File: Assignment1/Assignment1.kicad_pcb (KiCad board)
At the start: 2 copper layers, 50 x 50 mm, 22 parts, among them J1 Conn_01x02_Pin, J2 Conn_01x02_Pin, U1 TPS51386RJNR, U2 LD39200PU33R

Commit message: Update Assignment 1
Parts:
- removed Cbyp1: 470 nF, Capacitor_SMD:C_0603_1608Metric
- removed Cin1, Cout1: 10 uF, Capacitor_SMD:C_0603_1608Metric
- removed R_LDO_1: 56k, Resistor_SMD:R_0603_1608Metric
- removed R_LDO_2: 10k, Resistor_SMD:R_0603_1608Metric
- removed U2: LD39200PU33R, LD39200PU33R:SON95P300X300X100-7N
- added C2: 22pF, Capacitor_SMD:C_1210_3225Metric, F.Cu at (91.9, 83.8)
- added C3: 22pF, Capacitor_SMD:C_1210_3225Metric, F.Cu at (91.9, 80.3)
- added C8: 22pF, Capacitor_SMD:C_1210_3225Metric, F.Cu at (85.6, 83.9)
- added Cbyp2: 47 uF, Capacitor_SMD:C_1206_3216Metric, F.Cu at (73.3, 75.5)
- added Cin2: 1 uF, Capacitor_SMD:C_0603_1608Metric, F.Cu at (75.7, 85.1)
- added U3: ~, Package_TO_SOT_SMD:TO-263-3_TabPin2, F.Cu at (61.9, 83.3)
- C12: footprint Capacitor_SMD:C_0603_1608Metric -> Capacitor_SMD:C_1210_3225Metric
- C4, C5: footprint Capacitor_SMD:C_0603_1608Metric -> Capacitor_SMD:C_1206_3216Metric
- C7: value 100uF -> 22pF; footprint Capacitor_SMD:C_0603_1608Metric -> Capacitor_SMD:C_1210_3225Metric
- J1, J2: footprint Connector_PinSocket_2.54mm:PinSocket_1x02_P2.54mm_Vertical -> 5EHDVC-02P-KiCad:5EHDVC02P
- R4: value 150k -> 110k
- moved J1 38.3 mm to (89.6, 56.9), turned to 180 degrees
- moved C4 31.1 mm to (88.0, 63.3), turned to 180 degrees
- moved R3 29.2 mm to (93.3, 68.8), turned to 180 degrees
- moved C13 28.8 mm to (95.0, 70.6), turned to 0 degrees
- moved C5 28.3 mm to (88.0, 66.4), turned to 180 degrees
- moved J2 28.0 mm to (64.8, 56.5), turned to 0 degrees
- moved R1 27.1 mm to (95.1, 72.4), turned to 0 degrees
- moved C6 26.4 mm to (88.6, 68.6), turned to 180 degrees
- moved C1 26.1 mm to (95.2, 74.7), turned to 180 degrees
- moved U1 23.5 mm to (89.0, 71.7), turned to -90 degrees
- moved R6 19.5 mm to (81.0, 66.5)
- moved L1 19.3 mm to (88.9, 76.0), turned to -90 degrees
- moved R5 16.3 mm to (81.1, 68.8), turned to 180 degrees
- moved C7 15.4 mm to (85.6, 80.3), turned to 180 degrees
- moved R4 11.9 mm to (81.1, 71.4), turned to 180 degrees
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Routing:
- net /Buck_Vin: track 10.8 -> 0.00 mm
- net /Vout: track 9.98 -> 0.00 mm
- net Net-(U2-SENSE): track 7.18 -> 0.00 mm
- net /Buck_SW: track 6.28 -> 1.19 mm
- net Earth: track 7.67 -> 4.24 mm, vias 12 -> 36
- net /BuckStep_Vout: track 11.8 -> 14.3 mm
- net /Buck_VBST: track 3.27 -> 5.75 mm
- net /Buck_FB: track 8.46 -> 10.6 mm
- net /Buck_PG: track 10.3 -> 11.1 mm
- net Net-(C1-Pad1): track 1.80 -> 2.34 mm
- added copper zone on F.Cu, net /BuckStep_Vout
- added copper zone on F.Cu, net /Buck_SW
- added copper zone on F.Cu, net /Buck_Vin
- added copper zone on F.Cu, net /Vout

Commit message: fix smt
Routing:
- net /BuckStep_Vout: track 14.3 -> 0.00 mm
- net /Buck_PG: track 11.1 -> 0.00 mm, vias 2 -> 0
- net /Buck_FB: track 10.6 -> 0.00 mm
- net /Buck_Vcc: track 6.48 -> 0.00 mm
- net /Buck_VBST: track 5.75 -> 0.00 mm
- net Earth: track 4.24 -> 0.00 mm, vias 36 -> 0
- net Net-(C12-Pad1): track 3.06 -> 0.00 mm
- net Net-(C1-Pad1): track 2.34 -> 0.00 mm
- net /Buck_SW: track 1.19 -> 0.00 mm
- removed copper zone on F.Cu, net /BuckStep_Vout
- removed copper zone on F.Cu, net /Buck_SW
- removed copper zone on F.Cu, net /Buck_Vin
- removed copper zone on F.Cu, net /Vout
- removed copper zone on B.Cu, net Earth
- removed copper zone on F.Cu, net Earth

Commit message: generate BOM
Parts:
- moved Cbyp2 9.62 mm to (68.0, 67.5)
- moved U3 3.58 mm to (59.4, 80.8)
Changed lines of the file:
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@@
 	(footprint "Package_TO_SOT_SMD:TO-263-3_TabPin2"
 		(layer "F.Cu")
-		(at 61.946 83.312 180)
+		(at 59.425 80.775 180)
 		(descr "TO-263/D2PAK/DDPAK SMD package, http://www.infineon.com/cms/en/product/packages/PG-TO263/PG-TO263-3-1/")
 		(tags "D2PAK DDPAK TO-263 D2PAK-3 TO-263-3 SOT-404")
@@
 	(footprint "Capacitor_SMD:C_1206_3216Metric"
 		(layer "F.Cu")
-		(at 73.2518 75.5396)
+		(at 67.975 67.5)
 		(descr "Capacitor SMD 1206 (3216 Metric), square (rectangular) end terminal, IPC_7351 nominal, (Body size source: IPC-SM-782 page 76, https://www.pcb-3d.com/wordpress/wp-content/uploads/ipc-sm-782a_amendment_1_and_2.pdf), generated with kicad-footprint-generator")
 		(tags "capacitor")

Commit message: fix typo and update pcb
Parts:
- C2, C3, C7, C8: value 22pF -> 22uF
- moved C2 7.77 mm to (93.1, 91.5)
- moved C8 7.70 mm to (86.8, 91.5)
- moved C3 5.37 mm to (93.1, 85.5)
- moved C7 5.16 mm to (85.7, 85.5)
- moved R4 4.56 mm to (78.3, 75.0)
- moved C12 4.47 mm to (73.0, 71.0)
- moved C1 4.01 mm to (96.5, 78.5)
- moved L1 3.97 mm to (89.7, 79.9)
- moved U1 3.66 mm to (89.9, 75.2)
- moved C6 3.21 mm to (90.8, 71.0)
- moved R5 2.84 mm to (78.3, 69.5)
- moved R3 2.78 mm to (96.0, 68.0)
- moved R1 2.63 mm to (95.3, 75.0)
- moved C5 2.03 mm to (90.0, 67.0)
- moved R6 1.07 mm to (82.0, 67.0)
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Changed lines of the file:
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@@
 	(footprint "Resistor_SMD:R_0603_1608Metric"
 		(layer "F.Cu")
-		(at 93.345 68.834 180)
+		(at 96 68 180)
 		(descr "Resistor SMD 0603 (1608 Metric), square (rectangular) end terminal, IPC_7351 nominal, (Body size source: IPC-SM-782 page 72, https://www.pcb-3d.com/wordpress/wp-content/uploads/ipc-sm-782a_amendment_1_and_2.pdf), generated with kicad-footprint-generator")
 		(tags "resistor")
 		(property "Reference" "R3"
-			(at -2.667 0 0)
+			(at -0.675 1.5 0)
 			(layer "F.SilkS")
 			(effects
@@
 	(footprint "Capacitor_SMD:C_0603_1608Metric"
 		(layer "F.Cu")
-		(at 95.237 74.676 180)
+		(at 96.45 78.5 180)
 		(descr "Capacitor SMD 0603 (1608 Metric), square (rectangular) end terminal, IPC_7351 nominal, (Body size source: IPC-SM-782 page 76, https://www.pcb-3d.com/wordpress/wp-content/uploads/ipc-sm-782a_amendment_1_and_2.pdf), generated with kicad-footprint-generator")
 		(tags "capacitor")
@@
 	(footprint "Capacitor_SMD:C_1210_3225Metric"
 		(layer "F.Cu")
-		(at 85.607 83.893 180)
+		(at 86.782 91.5 180)
 		(descr "Capacitor SMD 1210 (3225 Metric), square (rectangular) end terminal, IPC_7351 nominal, (Body size source: IPC-SM-782 page 76, https://www.pcb-3d.com/wordpress/wp-content/uploads/ipc-sm-782a_amendment_1_and_2.pdf), generated with kicad-footprint-generator")
 		(tags "capacitor")
@@
 			)
 		)
-		(property "Value" "22pF"
+		(property "Value" "22uF"
 			(at 0 2.3 0)
 			(layer "F.Fab")
@@
 	(footprint "Resistor_SMD:R_0603_1608Metric"
 		(layer "F.Cu")
-		(at 81.09 68.834 180)
+		(at 78.325 69.5 180)
 		(descr "Resistor SMD 0603 (1608 Metric), square (rectangular) end terminal, IPC_7351 nominal, (Body size source: IPC-SM-782 page 72, https://www.pcb-3d.com/wordpress/wp-content/uploads/ipc-sm-782a_amendment_1_and_2.pdf), generated with kicad-footprint-generator")
 		(tags "resistor")
 		(property "Reference" "R5"
-			(at -2.603 0 0)
+			(at -3.778 -2.5 0)
 			(layer "F.SilkS")
 			(effects
@@
 		)
 		(property "Value" "0"
-			(at 0 1.43 0)
+			(at -1.175 -1.07 0)
 			(layer "F.Fab")
 			(effects
@@
 		)
 		(fp_text user "${REFERENCE}"
-			(at 0 0 0)
+			(at -1.175 -2.5 0)
 			(layer "F.Fab")
 			(effects
@@
 	(footprint "Capacitor_SMD:C_1210_3225Metric"
 		(layer "F.Cu")
-		(at 85.607 80.337 180)
+		(at 85.65 85.5 180)
 		(descr "Capacitor SMD 1210 (3225 Metric), square (rectangular) end terminal, IPC_7351 nominal, (Body size source: IPC-SM-782 page 76, https://www.pcb-3d.com/wordpress/wp-content/uploads/ipc-sm-782a_amendment_1_and_2.pdf), generated with kicad-footprint-generator")
 		(tags "capacitor")
@@
 			)
 		)
-		(property "Value" "22pF"
+		(property "Value" "22uF"
 			(at 0 2.3 0)
 			(layer "F.Fab")
@@
 	(footprint "Capacitor_SMD:C_1210_3225Metric"
 		(layer "F.Cu")
-		(at 91.948 83.82)
+		(at 93.123 91.5)
 		(descr "Capacitor SMD 1210 (3225 Metric), square (rectangular) end terminal, IPC_7351 nominal, (Body size source: IPC-SM-782 page 76, https://www.pcb-3d.com/wordpress/wp-content/uploads/ipc-sm-782a_amendment_1_and_2.pdf), generated with kicad-footprint-generator")
 		(tags "capacitor")
@@
 			)
 		)
-		(property "Value" "22pF"
+		(property "Value" "22uF"
 			(at 0 2.3 0)
 			(layer "F.Fab")
@@
 	(footprint "Capacitor_SMD:C_1210_3225Metric"
 		(layer "F.Cu")
-		(at 77.343 69.977 -90)
+		(at 73 71.025 -90)
 		(descr "Capacitor SMD 1210 (3225 Metric), square (rectangular) end terminal, IPC_7351 nominal, (Body size source: IPC-SM-782 page 76, https://www.pcb-3d.com/wordpress/wp-content/uploads/ipc-sm-782a_amendment_1_and_2.pdf), generated with kicad-footprint-generator")
 		(tags "capacitor")
@@
 	(footprint "Resistor_SMD:R_0603_1608Metric"
 		(layer "F.Cu")
-		(at 95.059 72.39)
+		(at 95.35 75)
 		(descr "Resistor SMD 0603 (1608 Metric), square (rectangular) end terminal, IPC_7351 nominal, (Body size source: IPC-SM-782 page 72, https://www.pcb-3d.com/wordpress/wp-content/uploads/ipc-sm-782a_amendment_1_and_2.pdf), generated with kicad-footprint-generator")
 		(tags "resistor")
@@
 	(footprint "Inductor_SMD:L_1210_3225Metric"
 		(layer "F.Cu")
-		(at 88.86 76.019 -90)
+		(at 89.675 79.9 -90)
 		(descr "Inductor SMD 1210 (3225 Metric), square (rectangular) end terminal, IPC_7351 nominal, (Body size source: http://www.tortai-tech.com/upload/download/2011102023233369053.pdf), generated with kicad-footprint-generator")
 		(tags "inductor")
@@
 	(footprint "Capacitor_SMD:C_1206_3216Metric"
 		(layer "F.Cu")
-		(at 88.049 66.367 180)
+		(at 89.975 67 180)
 		(descr "Capacitor SMD 1206 (3216 Metric), square (rectangular) end terminal, IPC_7351 nominal, (Body size source: IPC-SM-782 page 76, https://www.pcb-3d.com/wordpress/wp-content/uploads/ipc-sm-782a_amendment_1_and_2.pdf), generated with kicad-footprint-generator")
 		(tags "capacitor")
@@
 	(footprint "Capacitor_SMD:C_0603_1608Metric"
 		(layer "F.Cu")
-		(at 88.606 68.6308 180)
+		(at 90.775 71 180)
 		(descr "Capacitor SMD 0603 (1608 Metric), square (rectangular) end terminal, IPC_7351 nominal, (Body size source: IPC-SM-782 page 76, https://www.pcb-3d.com/wordpress/wp-content/uploads/ipc-sm-782a_amendment_1_and_2.pdf), generated with kicad-footprint-generator")
 		(tags "capacitor")
@@
 		)
 		(property "Value" "0.1 uF"
-			(at 3.797 -0.762 90)
+			(at 2.275 0 90)
 			(layer "F.Fab")
 			(effects
@@
 	(footprint "Capacitor_SMD:C_1210_3225Metric"
 		(layer "F.Cu")
-		(at 91.899 80.264)
+		(at 93.074 85.5)
 		(descr "Capacitor SMD 1210 (3225 Metric), square (rectangular) end terminal, IPC_7351 nominal, (Body size source: IPC-SM-782 page 76, https://www.pcb-3d.com/wordpress/wp-content/uploads/ipc-sm-782a_amendment_1_and_2.pdf), generated with kicad-footprint-generator")
 		(tags "capacitor")
@@
 			)
 		)
-		(property "Value" "22pF"
+		(property "Value" "22uF"
 			(at 0 2.3 0)
 			(layer "F.Fab")
@@
 	(footprint "Resistor_SMD:R_0603_1608Metric"
 		(layer "F.Cu")
-		(at 81.026 66.548)
+		(at 82 67)
 		(descr "Resistor SMD 0603 (1608 Metric), square (rectangular) end terminal, IPC_7351 nominal, (Body size source: IPC-SM-782 page 72, https://www.pcb-3d.com/wordpress/wp-content/uploads/ipc-sm-782a_amendment_1_and_2.pdf), generated with kicad-footprint-generator")
 		(tags "resistor")
@@
 	(footprint "TPS51386RJNR:VREG_TPS51386RJNR"
 		(layer "F.Cu")
-		(at 88.99 71.701 -90)
+		(at 89.9 75.25 -90)
 		(property "Reference" "U1"
 			(at -0.008 3.048 90)
@@
 		)
 		(property "Value" "TPS51386RJNR"
-			(at 0.5 5.842 90)
+			(at 0.25 4.4 90)
 			(layer "F.Fab")
 			(effects
@@
 	(footprint "Capacitor_SMD:C_0603_1608Metric"
 		(layer "F.Cu")
-		(at 94.983 70.612)
+		(at 95.45 71.5)
 		(descr "Capacitor SMD 0603 (1608 Metric), square (rectangular) end terminal, IPC_7351 nominal, (Body size source: IPC-SM-782 page 76, https://www.pcb-3d.com/wordpress/wp-content/uploads/ipc-sm-782a_amendment_1_and_2.pdf), generated with kicad-footprint-generator")
 		(tags "capacitor")
@@
 		)
 		(fp_text user "${REFERENCE}"
-			(at 0 0 0)
+			(at -1.175 -2.5 0)
 			(layer "F.Fab")
 			(effects
@@
 	(footprint "Resistor_SMD:R_0603_1608Metric"
 		(layer "F.Cu")
-		(at 81.089 71.374 180)
+		(at 78.325 75 180)
 		(descr "Resistor SMD 0603 (1608 Metric), square (rectangular) end terminal, IPC_7351 nominal, (Body size source: IPC-SM-782 page 72, https://www.pcb-3d.com/wordpress/wp-content/uploads/ipc-sm-782a_amendment_1_and_2.pdf), generated with kicad-footprint-generator")
 		(tags "resistor")
 		(property "Reference" "R4"
-			(at -2.604 0.127 0)
+			(at -3.779 -2.373 0)
 			(layer "F.SilkS")
 			(effects
@@
 		)
 		(fp_text user "${REFERENCE}"
-			(at 0 0 0)
+			(at -1.175 -2.5 0)
 			(layer "F.Fab")
 			(effects

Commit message: reformat
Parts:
- C13, Cin2: value 1 uF -> 1uF
- C4, C5: value 10 uF -> 10uF
- C6: value 0.1 uF -> 0.1uF
- Cbyp2: value 47 uF -> 47uF
- R3: value 100 k -> 100k
- moved C1 0.84 mm to (95.8, 79.0)
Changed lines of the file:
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@@
 			)
 		)
-		(property "Value" "100 k"
+		(property "Value" "100k"
 			(at -3.747 0 0)
 			(layer "F.Fab")
@@
 	(footprint "Capacitor_SMD:C_0603_1608Metric"
 		(layer "F.Cu")
-		(at 96.45 78.5 180)
+		(at 95.775 79 180)
 		(descr "Capacitor SMD 0603 (1608 Metric), square (rectangular) end terminal, IPC_7351 nominal, (Body size source: IPC-SM-782 page 76, https://www.pcb-3d.com/wordpress/wp-content/uploads/ipc-sm-782a_amendment_1_and_2.pdf), generated with kicad-footprint-generator")
 		(tags "capacitor")
@@
 		(tags "resistor")
 		(property "Reference" "R5"
-			(at -3.778 -2.5 0)
+			(at -0.175 1.5 0)
 			(layer "F.SilkS")
 			(effects
@@
 		)
 		(property "Value" "0"
-			(at -1.175 -1.07 0)
+			(at -0.175 -1.5 0)
 			(layer "F.Fab")
 			(effects
@@
 		)
 		(fp_text user "${REFERENCE}"
-			(at -1.175 -2.5 0)
+			(at 0 0 0)
 			(layer "F.Fab")
 			(effects
@@
 			)
 		)
-		(property "Value" "10 uF"
+		(property "Value" "10uF"
 			(at 2.999 0 90)
 			(layer "F.Fab")
@@
 			)
 		)
-		(property "Value" "0.1 uF"
+		(property "Value" "0.1uF"
 			(at 2.275 0 90)
 			(layer "F.Fab")
@@
 			)
 		)
-		(property "Value" "1 uF"
+		(property "Value" "1uF"
 			(at 0 1.43 0)
 			(layer "F.Fab")
@@
 			)
 		)
-		(property "Value" "1 uF"
+		(property "Value" "1uF"
 			(at 0 1.43 90)
 			(layer "F.Fab")
@@
 			)
 		)
-		(property "Value" "10 uF"
+		(property "Value" "10uF"
 			(at 2.999 0 90)
 			(layer "F.Fab")
@@
 		)
 		(fp_text user "${REFERENCE}"
-			(at -1.175 -2.5 0)
+			(at 0 0 0)
 			(layer "F.Fab")
 			(effects
@@
 			)
 		)
-		(property "Value" "47 uF"
+		(property "Value" "47uF"
 			(at 0 1.85 0)
 			(layer "F.Fab")
@@
 		(tags "resistor")
 		(property "Reference" "R4"
-			(at -3.779 -2.373 0)
+			(at -0.175 -1.5 0)
 			(layer "F.SilkS")
 			(effects
@@
 		)
 		(fp_text user "${REFERENCE}"
-			(at -1.175 -2.5 0)
+			(at 0 0 0)
 			(layer "F.Fab")
 			(effects

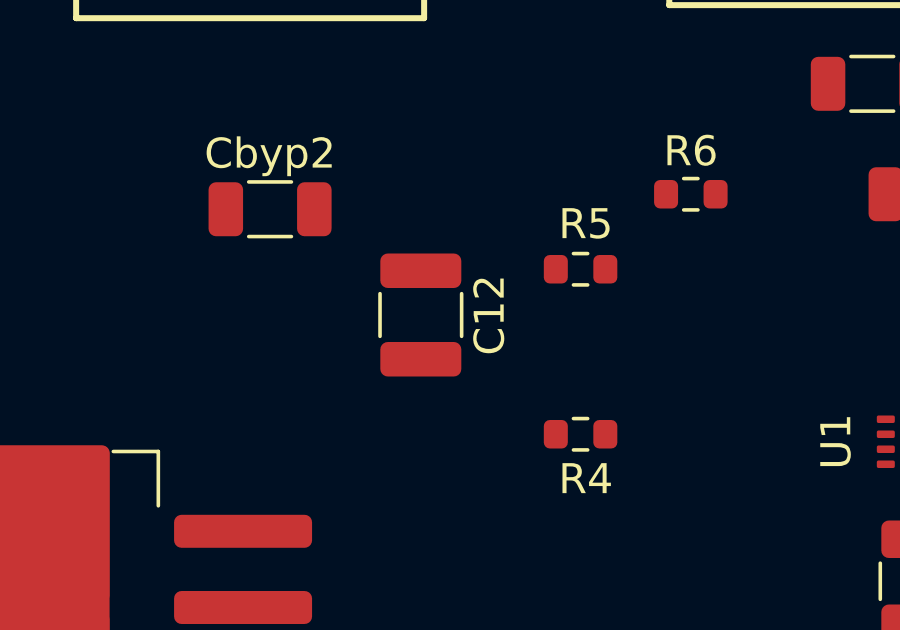
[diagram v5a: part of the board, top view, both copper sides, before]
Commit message: update C 22pf package size to 0603
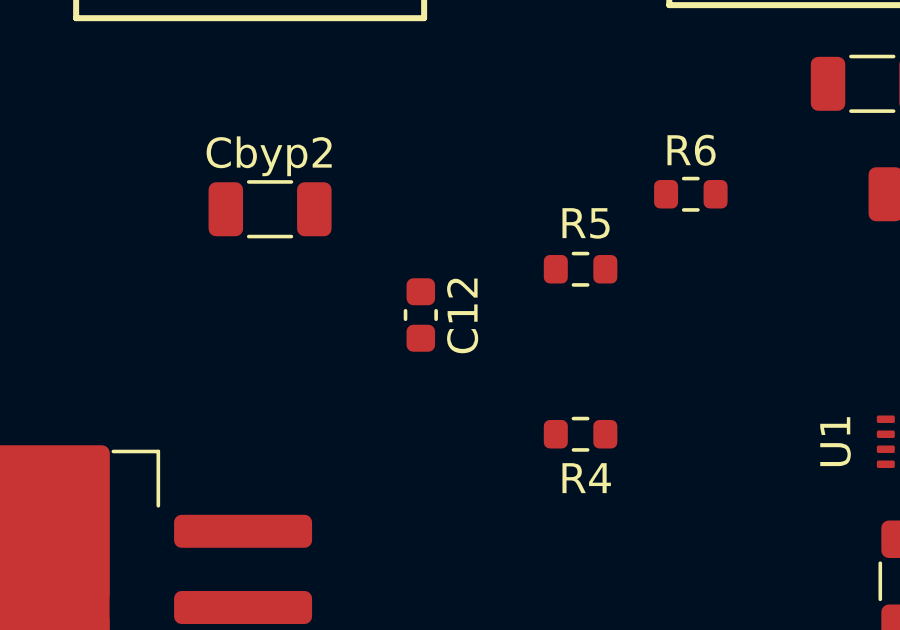
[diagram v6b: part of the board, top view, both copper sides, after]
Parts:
- C12: footprint Capacitor_SMD:C_1210_3225Metric -> Capacitor_SMD:C_0603_1608Metric
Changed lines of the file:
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@@
 		)
 	)
-	(footprint "Capacitor_SMD:C_1210_3225Metric"
+	(footprint "Capacitor_SMD:C_0603_1608Metric"
 		(layer "F.Cu")
 		(at 73 71.025 -90)
-		(descr "Capacitor SMD 1210 (3225 Metric), square (rectangular) end terminal, IPC_7351 nominal, (Body size source: IPC-SM-782 page 76, https://www.pcb-3d.com/wordpress/wp-content/uploads/ipc-sm-782a_amendment_1_and_2.pdf), generated with kicad-footprint-generator")
+		(descr "Capacitor SMD 0603 (1608 Metric), square (rectangular) end terminal, IPC_7351 nominal, (Body size source: IPC-SM-782 page 76, https://www.pcb-3d.com/wordpress/wp-content/uploads/ipc-sm-782a_amendment_1_and_2.pdf), generated with kicad-footprint-generator")
 		(tags "capacitor")
 		(property "Reference" "C12"
-			(at 0 -2.3 90)
+			(at 0 -1.43 -90)
 			(layer "F.SilkS")
 			(effects
@@
 		)
 		(property "Value" "22pF"
-			(at 0 2.3 90)
-			(layer "F.Fab")
-			(effects
-				(font
-					(size 1 1)
-					(thickness 0.15)
-				)
-			)
-		)
-		(property "Footprint" "Capacitor_SMD:C_1210_3225Metric"
-			(at 0 0 90)
+			(at 0 1.43 -90)
+			(layer "F.Fab")
+			(effects
+				(font
+					(size 1 1)
+					(thickness 0.15)
+				)
+			)
+		)
+		(property "Footprint" "Capacitor_SMD:C_0603_1608Metric"
+			(at 0 0 -90)
+			(unlocked yes)
 			(layer "F.Fab")
 			(hide yes)
@@
 		)
 		(property "Datasheet" ""
-			(at 0 0 90)
+			(at 0 0 -90)
+			(unlocked yes)
 			(layer "F.Fab")
 			(hide yes)
@@
 		)
 		(property "Description" ""
-			(at 0 0 90)
+			(at 0 0 -90)
+			(unlocked yes)
 			(layer "F.Fab")
 			(hide yes)
@@
 		(attr smd)
 		(fp_line
-			(start -0.711252 1.36)
-			(end 0.711252 1.36)
+			(start -0.14058 0.51)
+			(end 0.14058 0.51)
 			(stroke
 				(width 0.12)
@@
 		)
 		(fp_line
-			(start -0.711252 -1.36)
-			(end 0.711252 -1.36)
+			(start -0.14058 -0.51)
+			(end 0.14058 -0.51)
 			(stroke
 				(width 0.12)
@@
 		)
 		(fp_line
-			(start -2.3 1.6)
-			(end -2.3 -1.6)
+			(start -1.48 0.73)
+			(end -1.48 -0.73)
 			(stroke
 				(width 0.05)
@@
 		)
 		(fp_line
-			(start 2.3 1.6)
-			(end -2.3 1.6)
+			(start 1.48 0.73)
+			(end -1.48 0.73)
 			(stroke
 				(width 0.05)
@@
 		)
 		(fp_line
-			(start -2.3 -1.6)
-			(end 2.3 -1.6)
+			(start -1.48 -0.73)
+			(end 1.48 -0.73)
 			(stroke
 				(width 0.05)
@@
 		)
 		(fp_line
-			(start 2.3 -1.6)
-			(end 2.3 1.6)
+			(start 1.48 -0.73)
+			(end 1.48 0.73)
 			(stroke
 				(width 0.05)
@@
 		)
 		(fp_line
-			(start -1.6 1.25)
-			(end -1.6 -1.25)
+			(start -0.8 0.4)
+			(end -0.8 -0.4)
 			(stroke
 				(width 0.1)
@@
 		)
 		(fp_line
-			(start 1.6 1.25)
-			(end -1.6 1.25)
+			(start 0.8 0.4)
+			(end -0.8 0.4)
 			(stroke
 				(width 0.1)
@@
 		)
 		(fp_line
-			(start -1.6 -1.25)
-			(end 1.6 -1.25)
+			(start -0.8 -0.4)
+			(end 0.8 -0.4)
 			(stroke
 				(width 0.1)
@@
 		)
 		(fp_line
-			(start 1.6 -1.25)
-			(end 1.6 1.25)
+			(start 0.8 -0.4)
+			(end 0.8 0.4)
 			(stroke
 				(width 0.1)
@@
 		)
 		(fp_text user "${REFERENCE}"
-			(at 0 0 90)
-			(layer "F.Fab")
-			(effects
-				(font
-					(size 0.8 0.8)
-					(thickness 0.12)
+			(at 0 0 -90)
+			(layer "F.Fab")
+			(effects
+				(font
+					(size 0.4 0.4)
+					(thickness 0.06)
 				)
 			)
 		)
 		(pad "1" smd roundrect
-			(at -1.475 0 270)
-			(size 1.15 2.7)
+			(at -0.775 0 270)
+			(size 0.9 0.95)
 			(layers "F.Cu" "F.Paste" "F.Mask")
-			(roundrect_rratio 0.217391)
+			(roundrect_rratio 0.25)
 			(net 6 "Net-(C12-Pad1)")
 			(pintype "passive")
 		)
 		(pad "2" smd roundrect
-			(at 1.475 0 270)
-			(size 1.15 2.7)
+			(at 0.775 0 270)
+			(size 0.9 0.95)
 			(layers "F.Cu" "F.Paste" "F.Mask")
-			(roundrect_rratio 0.217391)
+			(roundrect_rratio 0.25)
 			(net 5 "/BuckStep_Vout")
 			(pintype "passive")
 		)
-		(model "${KICAD6_3DMODEL_DIR}/Capacitor_SMD.3dshapes/C_1210_3225Metric.wrl"
+		(model "${KICAD8_3DMODEL_DIR}/Capacitor_SMD.3dshapes/C_0603_1608Metric.wrl"
 			(offset
 				(xyz 0 0 0)
